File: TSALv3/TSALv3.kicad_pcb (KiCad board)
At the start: 2 copper layers, 71.6 x 42.7 mm, 42 parts, among them J1 Conn_01x06_Female, J2 HV, Q1 2N7002, Q2 MCT06P10-TP, Q3 2N7002, Q4 MCT06P10-TP, U1 SPAN02A-12, U2 LM311, U3 4N35, U4 NE555

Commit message: cleanup TSALv3 models
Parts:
- J1: footprint Connector_Molex:Molex_Micro-Fit_3.0_43045-0600_2x03_P3.00mm_Horizontal -> Connector_Molex:Molex_Micro-Fit_3.0_43045-0612_2x03_P3.00mm_Vertical
- moved J1 5.94 mm to (116.2, 70.1)
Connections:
- J1 pad 2: GLV- -> /GRN+
- J1 pad 4: /GRN+ -> GLV-
- R10 pad 2: /Vref -> /Vin
- R11 pad 2: /Vin -> /Vref
- R12 pad 1: /Vref -> /Vin
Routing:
- net /Vref: track 24.8 -> 11.9 mm
- net /Vin: track 21.5 -> 34.2 mm, vias 1 -> 2
- net /GRN+: track 12.0 -> 20.7 mm
- net GND: track 101.0 -> 93.3 mm, vias 0 -> 2
- net /RED+: track 53.0 -> 47.8 mm
- net GLV+: track 24.2 -> 28.8 mm
- net GLV-: vias 5 -> 6
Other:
- board text added: "+"
- board text added: "DON'T PANIC"
- board text added: "G+"
- board text added: "G-"
- board text added: "GLV+"
- board text added: "GLV-"
- board text added: "R+"
- board text added: "R-"

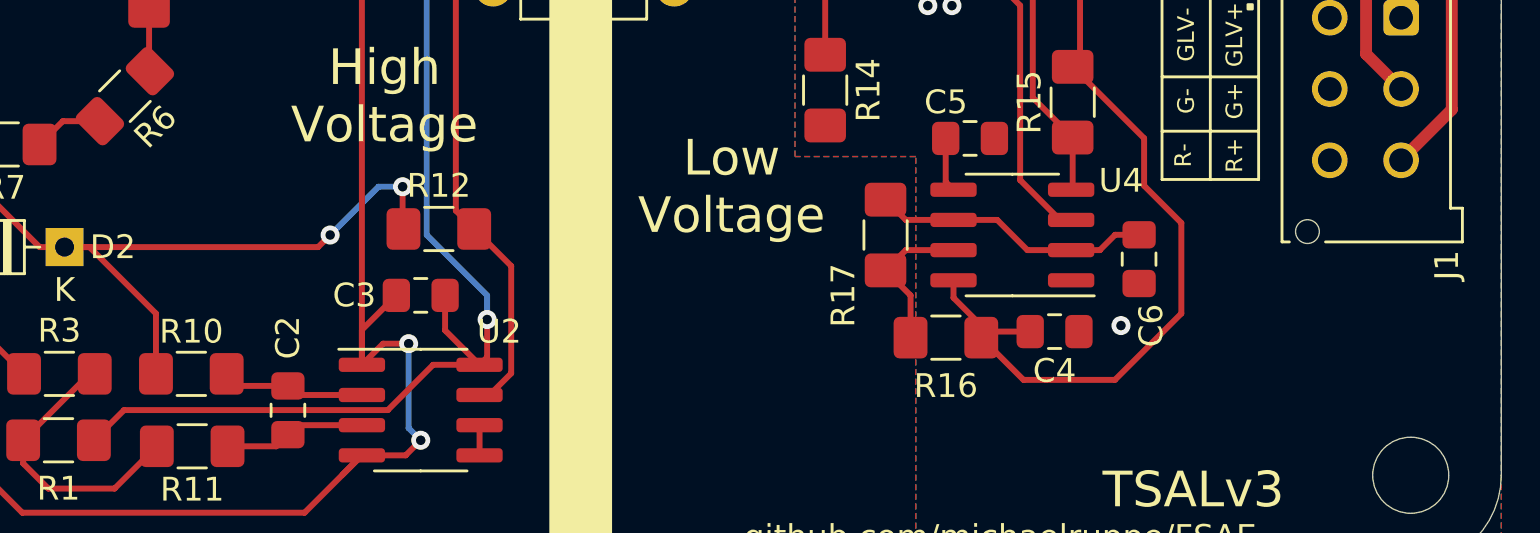
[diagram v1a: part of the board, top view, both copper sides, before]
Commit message: Documentation, aesthetic upgrades
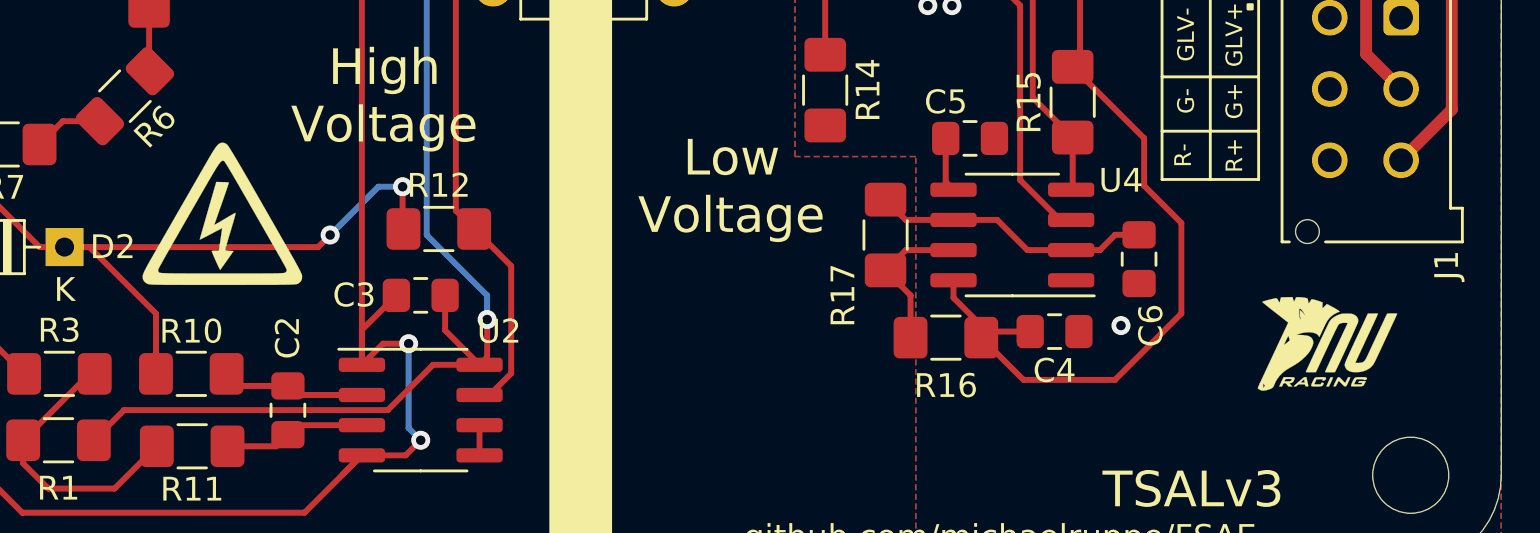
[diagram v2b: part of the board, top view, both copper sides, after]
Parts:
- added G***: LOGO, TSAL-HVM:electric-shock-symbol, F.Cu at (66.6, 78.4)
- added G***: LOGO, TSAL-HVM:logo, F.Cu at (113.1, 83.9)

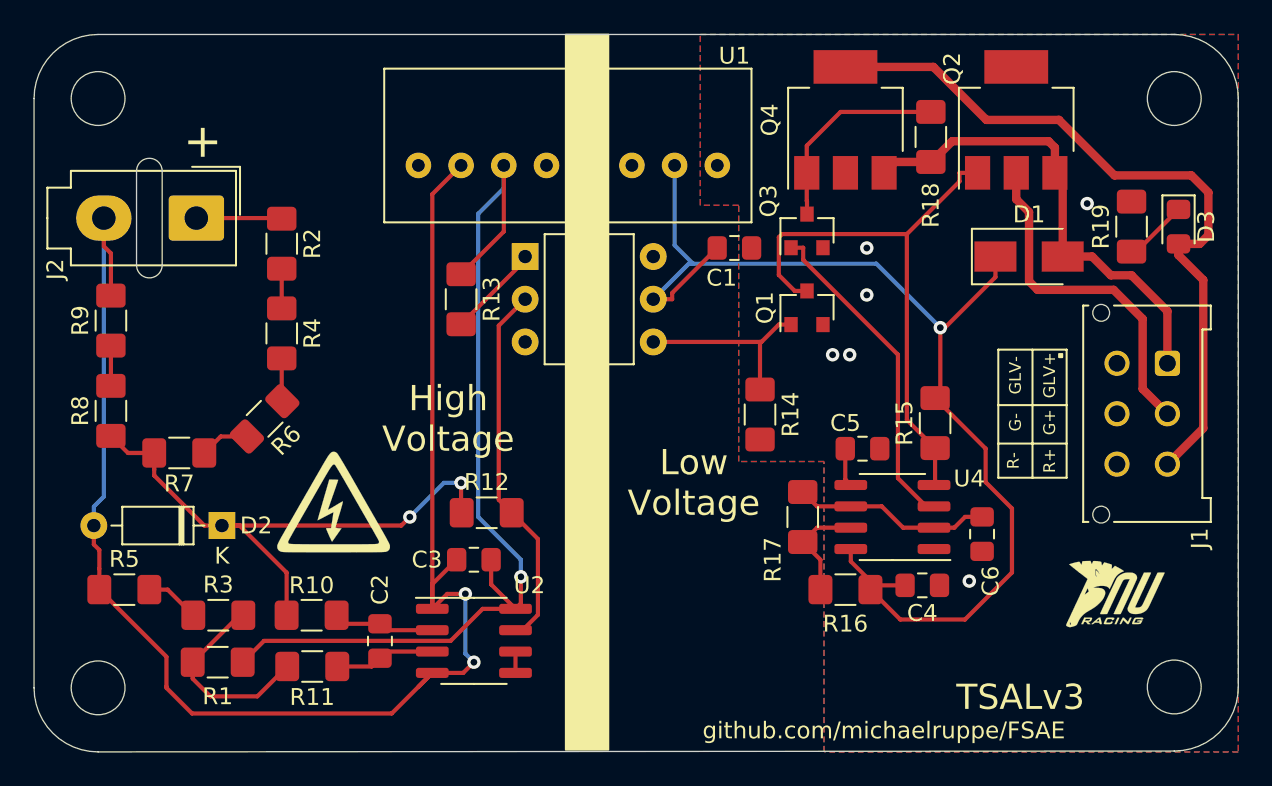
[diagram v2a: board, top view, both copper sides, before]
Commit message: update project for KiCad 9.x
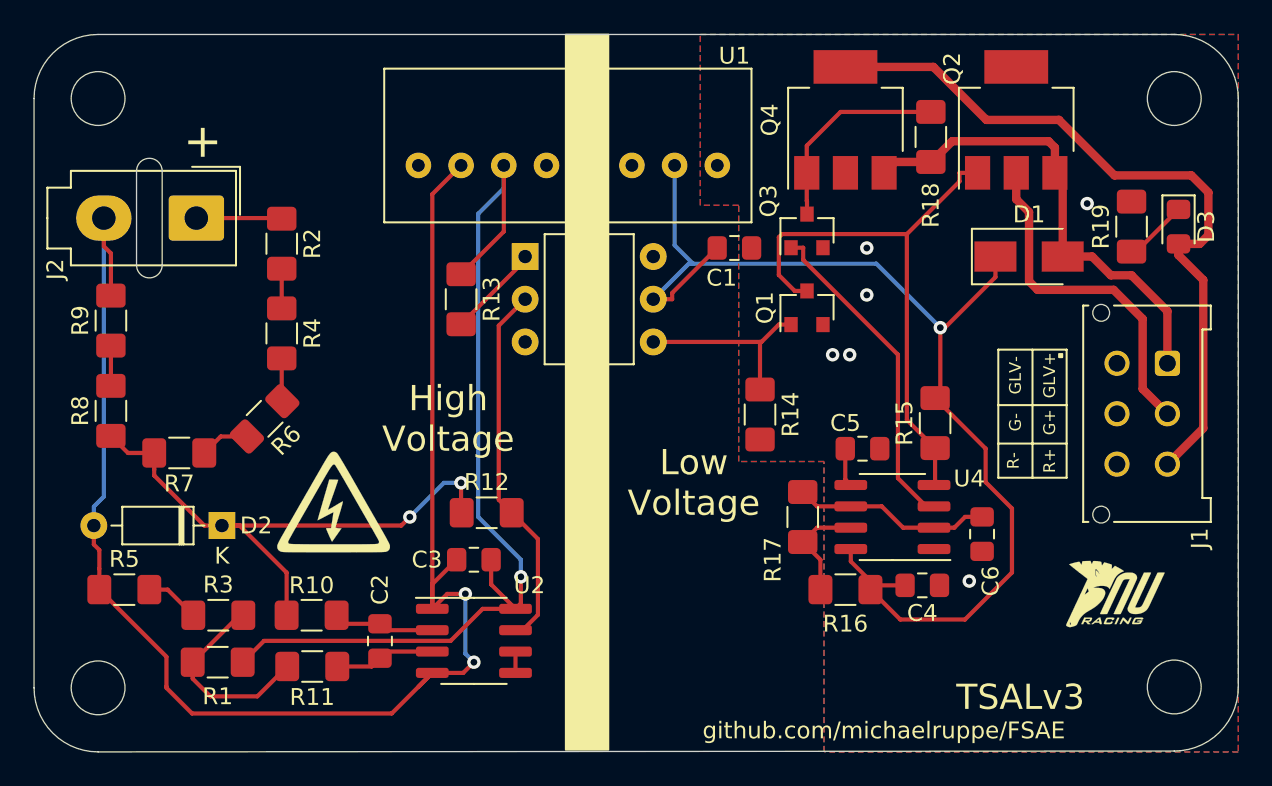
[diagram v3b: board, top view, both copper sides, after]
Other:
- net class Default removed
